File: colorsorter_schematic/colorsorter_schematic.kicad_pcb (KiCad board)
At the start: 2 copper layers, 34 parts, among them J1 Conn_01x03_Pin, J2 Conn_01x03_Pin, J3 Conn_01x03_Pin, J4 Conn_01x05_Pin, J5 Conn_01x05_Pin, J6 Conn_01x03_Pin, J7 Conn_01x03_Pin, SW1 SW_SPDT, U1 PIC24FJ64GA702-I/SO, U2 ESP8266-01_ESP-01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

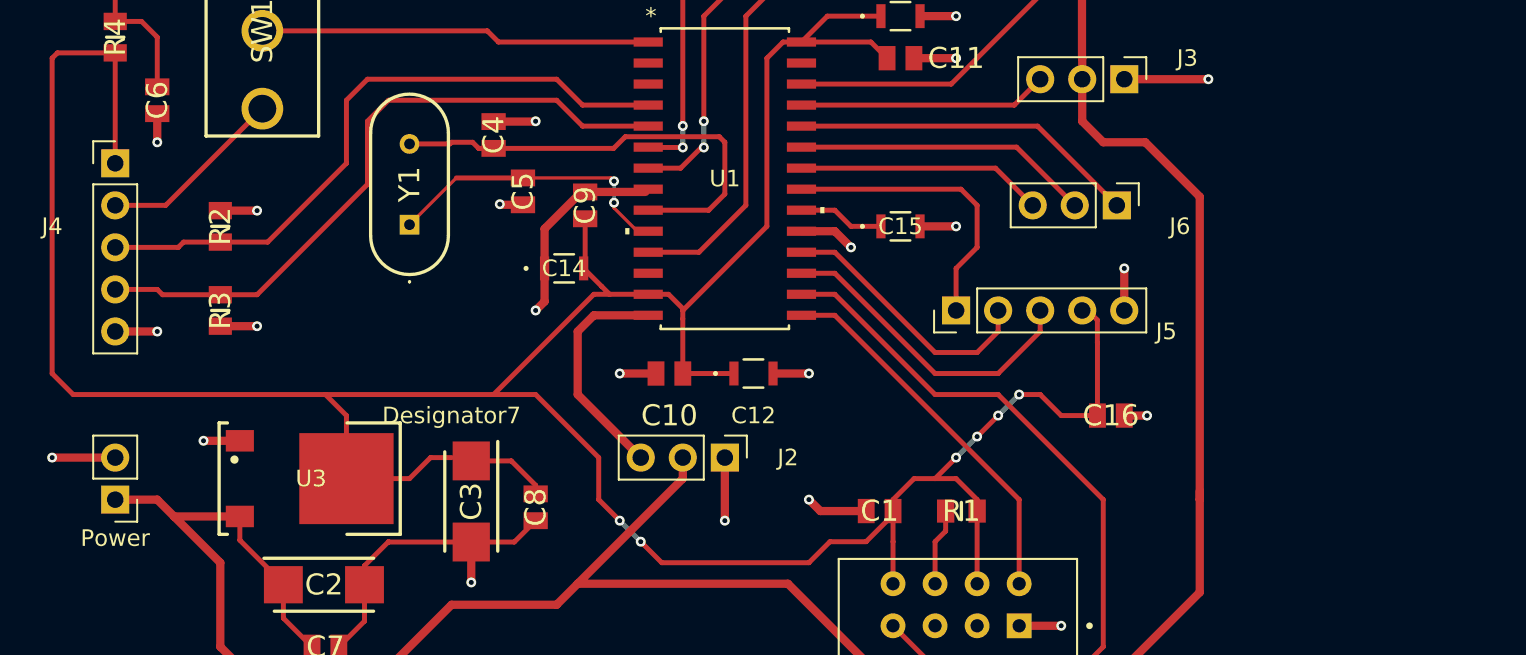
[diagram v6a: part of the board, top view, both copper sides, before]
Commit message: J5 conn changed from 5 pin to 6 pin - updated pcb - saved changes
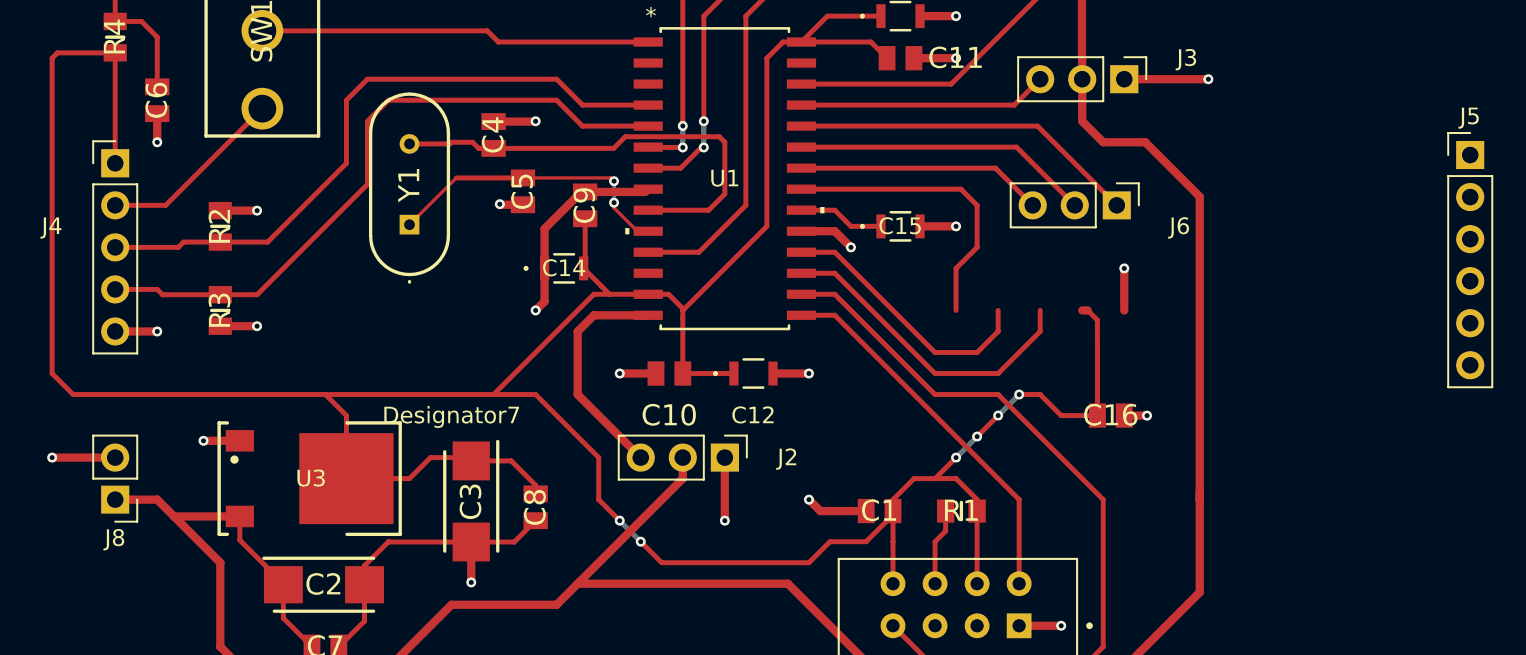
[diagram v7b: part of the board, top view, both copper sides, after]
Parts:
- J5: value Conn_01x05_Pin -> Conn_01x06_Pin; footprint Connector_PinHeader_2.54mm:PinHeader_1x05_P2.54mm_Vertical -> Connector_PinHeader_2.54mm:PinHeader_1x06_P2.54mm_Vertical
- moved J5 32.4 mm to (196.2, 91.3), turned to 0 degrees
- renumbered Power to J8
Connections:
- J5 pad 1: Net-(J5-Pin_1) -> Net-(C2-+)
- J5 pad 2: /SDA -> Net-(J5-Pin_2)
- J5 pad 3: /SCL -> /SDA
- J5 pad 4: Net-(C3-+) -> /SCL
- J5 pad 5: GND -> Net-(C3-+)
- U1 pad 21: Net-(J5-Pin_1) -> Net-(J5-Pin_2)
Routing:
- net Net-(J5-Pin_2): track 0.00 -> 17.9 mm
- net Net-(J5-Pin_1): track 17.9 -> 0.00 mm

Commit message: Dodavanje izmjena na pcb projekta
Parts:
- moved J5 32.9 mm to (164.3, 99.7), turned to 90 degrees
- moved C9 1.54 mm to (141.7, 95.5), turned to 180 degrees
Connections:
- J5 pad 1: Net-(C2-+) -> Net-(J5-Pin_1)
- J5 pad 3: /SDA -> /SCL
- J5 pad 4: /SCL -> Net-(C3-+)
- J5 pad 5: Net-(C3-+) -> GND
- J5 pad 6: GND -> Net-(C2-+)
- U1 pad 18: /SDA -> Net-(J5-Pin_2)
- U1 pad 21: Net-(J5-Pin_2) -> Net-(J5-Pin_1)
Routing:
- net GND: track 89.4 -> 64.7 mm
- net /SDA: track 16.2 -> 0.00 mm
- net Net-(J5-Pin_1): track 0.00 -> 16.0 mm
- net Net-(C2-+): track 147.8 -> 152.2 mm
- net Net-(J5-Pin_2): track 17.9 -> 16.4 mm
- net Net-(U1-OSCO/CLKO/C2IND/RA3): track 17.9 -> 16.9 mm, vias 2 -> 0
- net /SCL: track 19.8 -> 20.5 mm
- net Net-(C3-+): track 198.7 -> 199.4 mm
- net Net-(J1-Pin_3): track 17.9 -> 18.5 mm
